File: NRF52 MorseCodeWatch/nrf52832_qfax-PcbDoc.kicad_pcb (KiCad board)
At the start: 2 copper layers, 28.2 x 34.8 mm, 46 parts, among them J2 USB_B_Micro, J3 Conn_01x02_Male LiPo Battery, J5 BatteryHolder_Keystone_3034_1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, M1 Motor_DC, M2 Motor_DC, SW1 SW_DIP_x01, U1 NRF52832-QFAA-R, U2 AT42QT1010-TSHR, U3 CAT24C256, U4 MCP73831-2-OT, U5 DRV8836, X1 32mHz, X2 32.768kHz

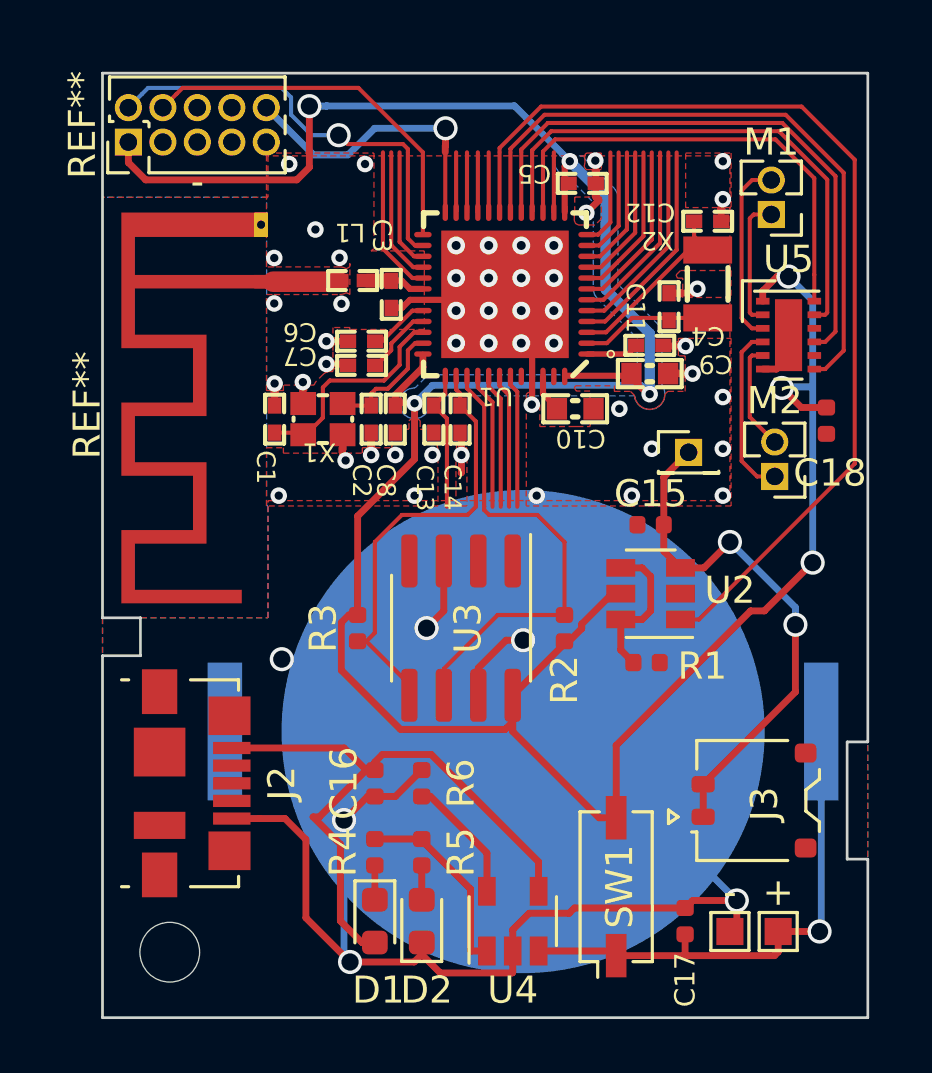
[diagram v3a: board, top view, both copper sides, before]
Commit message: update PCB with voltage regulator
using a voltage regulator now with the PCB design.

update BOM
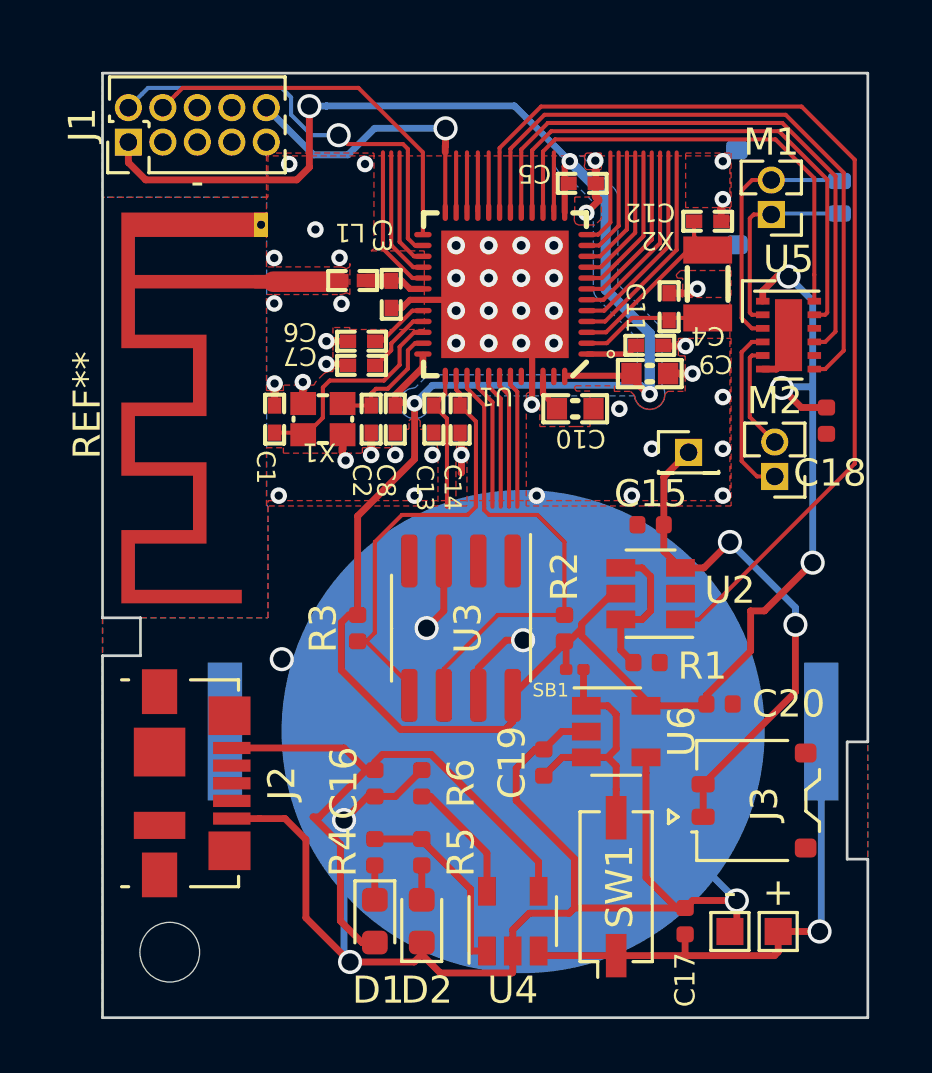
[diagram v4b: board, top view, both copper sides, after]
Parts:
- added C19: C 1uf, Capacitor_SMD:C_0402_1005Metric, F.Cu at (100.8, 88.1)
- added C20: C 2.2uf, Capacitor_SMD:C_0402_1005Metric, F.Cu at (107.3, 86.0)
- added J6: Conn_01x02_Male LiPo Battery, Connector_JST:JST_ACH_BM02B-ACHSS-GAN-ETF_1x02-1MP_P1.20mm_Vertical, B.Cu at (109.9, 67.3)
- added SB1: R_0201_0603Metric, Resistor_SMD:R_0201_0603Metric, F.Cu at (102.0, 84.7)
- added U6: TPS783, Package_TO_SOT_SMD:SOT-23-5, F.Cu at (103.5, 87.0)
- J5: value BatteryHolder_Keystone_3034_1x20mm -> Battery_Cell
- R4, R5: value R -> R 47Ω
- renumbered REF** to J1
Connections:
- SW1 pad 2: /VDD_nRF -> /VDD_in
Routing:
- net GND: track 80.9 -> 96.4 mm, vias 55 -> 54
- net /VDD_in: track 0.00 -> 9.31 mm
- net /VDD_nRF: track 108.2 -> 104.3 mm
- net /Motor1_out: track 4.84 -> 7.36 mm
- net /Motor1_outB: track 6.89 -> 9.41 mm
- net (no net): vias 0 -> 1
